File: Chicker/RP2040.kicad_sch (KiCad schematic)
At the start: 44 parts, among them J2 USB4145-03-0170-C_REVA2, J4 JST_2P_LIMITSW, J5 Conn_02x09_Counter_Clockwise, U1 RPI2040, U10 PTS647SM38SMTR2LFS, U5 W25Q16JVSNIQ, U9 PTS647SM38SMTR2LFS, Y1 ABM3-12.000MHZ-D2Y-T

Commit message: chicker v1.1 basic parts
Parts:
- removed D21, D22, D23, D24, D25: BZT52C3V3T-7, bots:D_SOD-523, symbol thebots_symlib:D_ZENER_BZT52C3V3T-7
- removed D5: SMBJ5338B-TP, bots:D_SMB, symbol bots:D_ZENER_SMBJ5338B-TP
- removed U10, U9: PTS647SM38SMTR2LFS, bots:SW_PTS647SM38SMTR2LFS_CNK, symbol bots:PTS647SM38SMTR2LFS
- removed U5: W25Q16JVSNIQ, bots:SOIC-8_3.9x4.9mm_P1.27mm, symbol bots:W25Q16JVSNIQ
- removed Y1: ABM3-12.000MHZ-D2Y-T, bots:ABM3, symbol bots:ABM3-12.000MHZ-D2Y-T
- added D21, D23: ESD7C3.3DT5G-MS, bots:SOT-723, symbol bots:D_TVS_ESD
- added D5: SMBJ5338B-TP_alternate, bots:D_SMB, symbol bots:D_ZENER_SMBJ5338B_alternate
- added U10, U9: SW_TS-1187A-B-A-B, bots:SW_TS-1187A-B-A-B, symbol bots:SW_TS-1187A-B-A-B
- added U5: W25Q128JVSIQ, bots:SOIC-8_208mil, symbol bots:W25Q128JVSIQ
- added Y1: XTAL-12MHZ-YXC, bots:SMD3225-4P, symbol bots:XTAL-12MHZ-YXC
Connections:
- net +3.3V: now also U5.8 (VCC)
- net 5V_LEVEL: now also D21.2
- net 5V_USB: now also D5.1 (K)
- net BATT_LEVEL: now also D21.1
- net BKBM: now also D23.1
- net BOOT: now also U10.1, U10.2
- net CHIP: now also D21.1
- net GND: now also D21.3, D23.3, D5.2 (A), U10.3, U10.4, U5.4 (GND), U9.3, U9.4, Y1.2, Y1.4
- net GPIO27_ADC2: now also D23.2
- net KICK: now also D21.2
- net QSPI_SCLK: now also U5.6 (CLK)
- net QSPI_SD0: now also U5.5 (DI(IO0))
- net QSPI_SD1: now also U5.2 (DO(IO1))
- net QSPI_SD2: now also U5.3 (IO2)
- net QSPI_SD3: now also U5.7 (IO3)
- net QSPI_SS: now also U5.1 (~{CS})
- net RUN: now also U9.1, U9.2
- net XIN: now also Y1.3
- net XOUT_R: now reaches C25.2, R17.1
- net XOUT_R: now also Y1.1
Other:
- moved on the sheet: R17

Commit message: more parts
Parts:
- added D21: ESD7C3.3DT5G-MS, bots:SOT-723, symbol bots:D_TVS_ESD
- renumbered D21 to D22
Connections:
- net CHIP: now also D21.1; no longer D22.1
- net GND: now also D21.3
- net KICK: now also D21.2; no longer D22.2

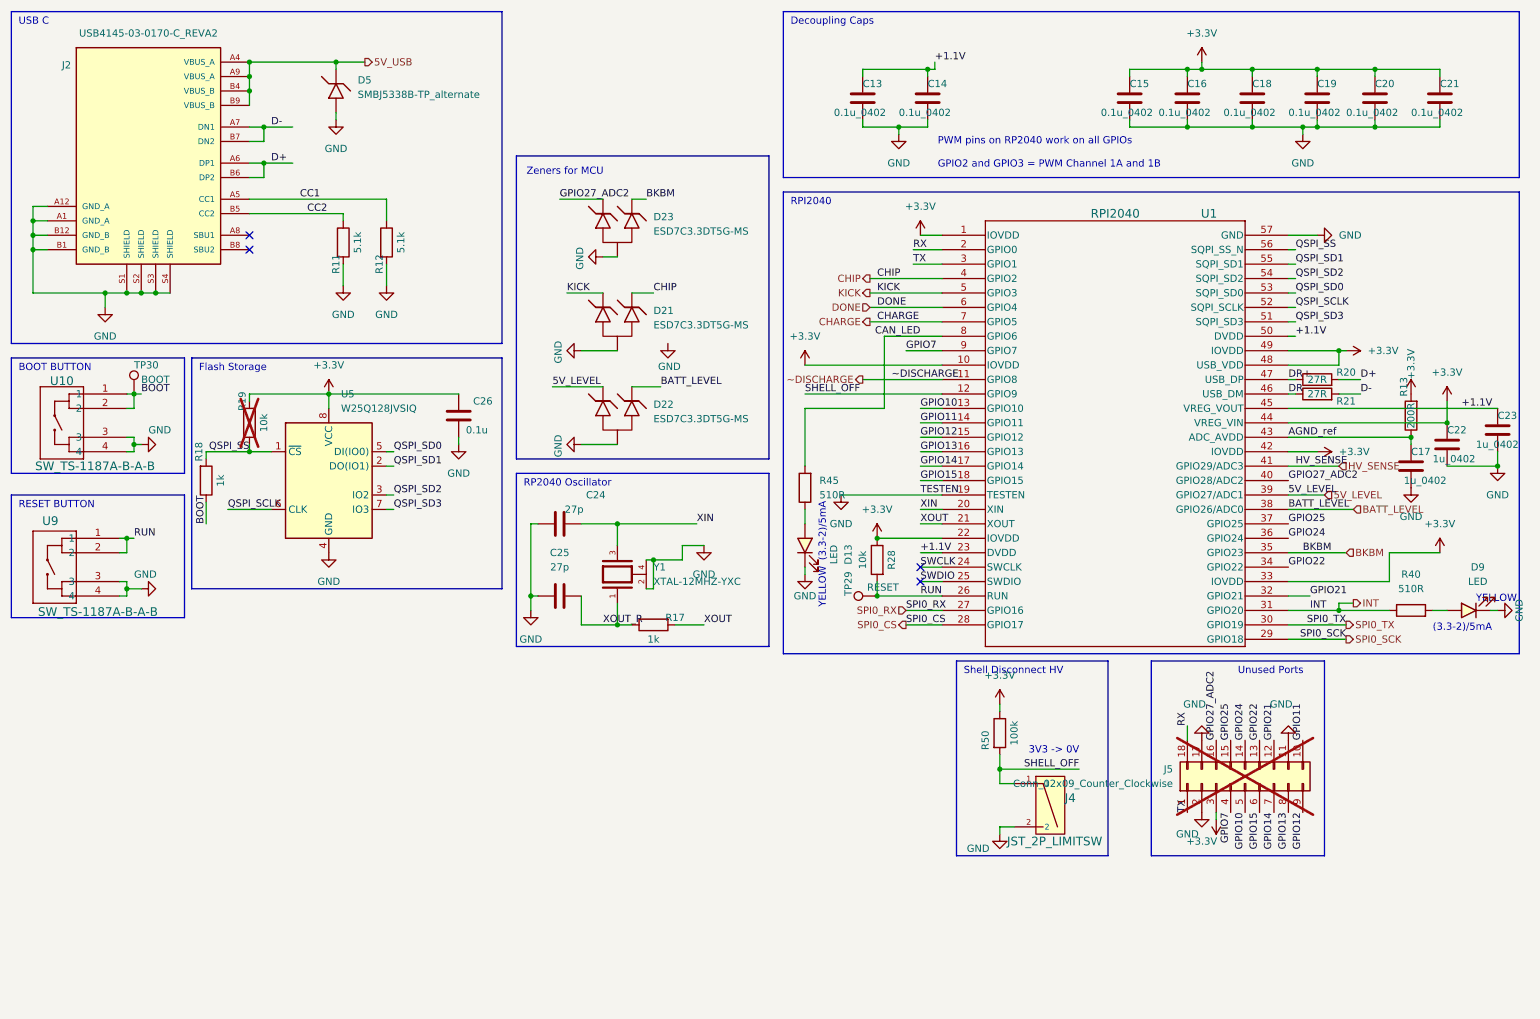
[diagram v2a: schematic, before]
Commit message: changed more to basic
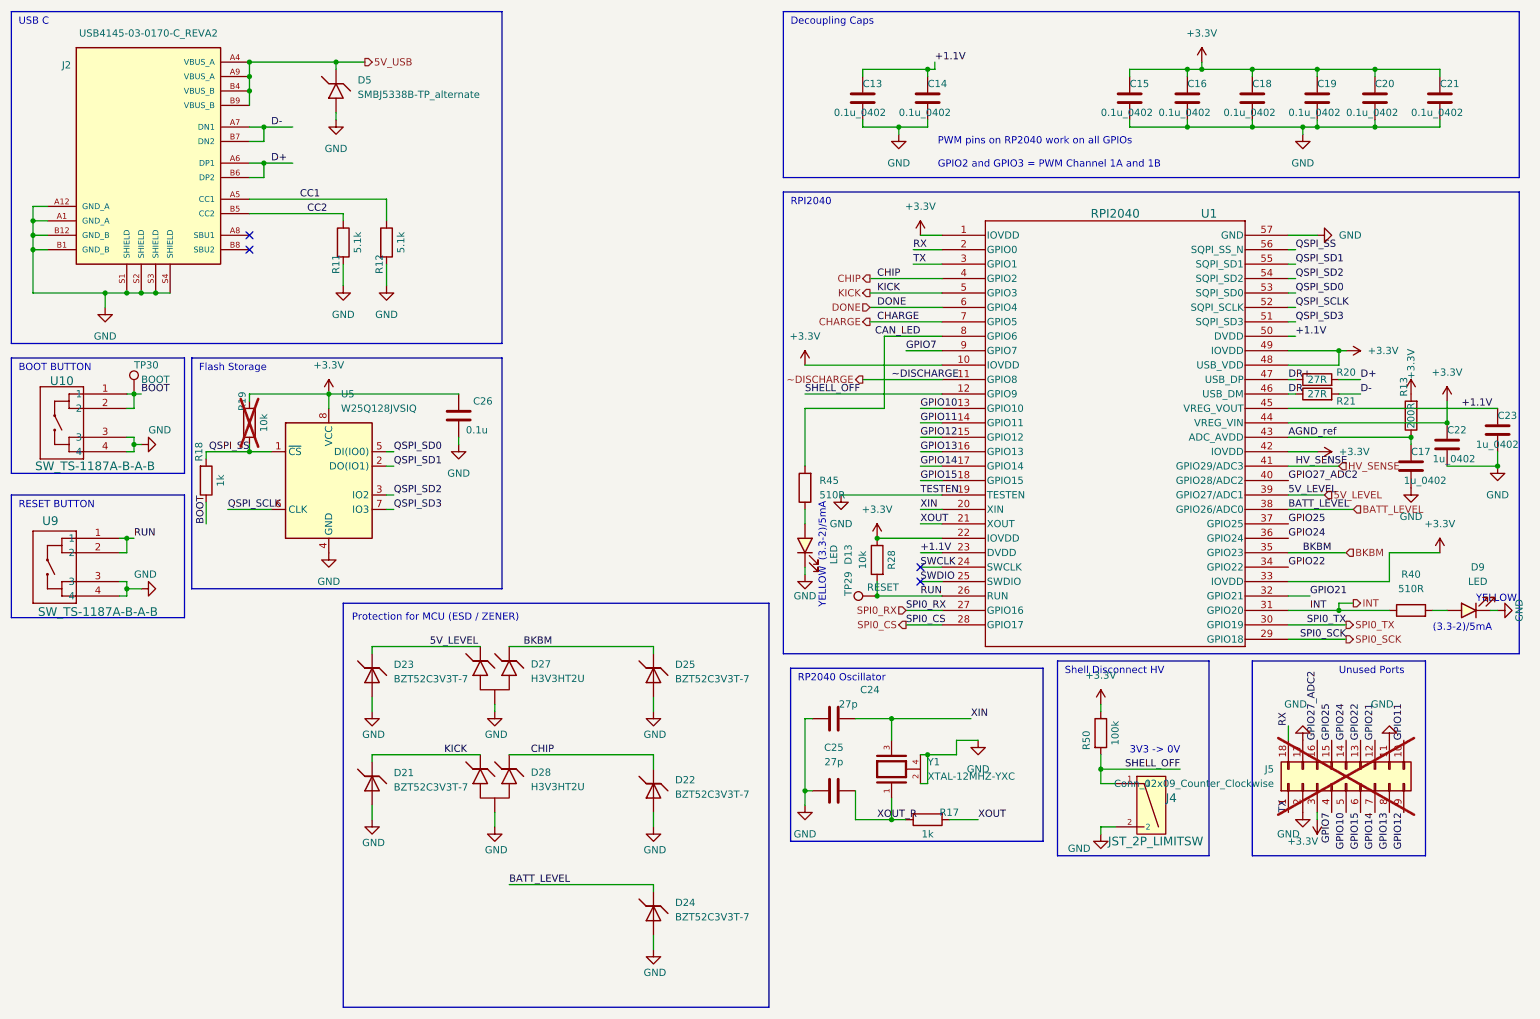
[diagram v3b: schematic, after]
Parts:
- removed D22: ESD7C3.3DT5G-MS, bots:SOT-723, symbol bots:D_TVS_ESD
- added D21, D22, D23, D24, D25: BZT52C3V3T-7, bots:D_SOD-523, symbol bots:D_ZENER_BZT52C3V3T-7_alternate
- D13, D9: footprint bots:LED_0603_1608Metric -> bots:LED_0805_2012Metric; JLC 0603 -> 0805; LCSC C72038 -> C2296; MPN 19-213/Y2C-CQ2R2L/3T(CY) -> KT-0805Y; Manufacturer Everlight Elec -> Hubei KENTO Elec
- D27: renamed from D23; value ESD7C3.3DT5G-MS -> H3V3HT2U; JLC SOT-723 -> SOT-23; LCSC C5331072 -> C20617924; MPN ESD7C3.3DT5G-MS -> H3V3HT2U; Manufacturer Micro Commercial Co -> hongjiacheng; Price 0.63 -> 0.0379
- D28: renamed from D21; value ESD7C3.3DT5G-MS -> H3V3HT2U; JLC SOT-723 -> SOT-23; LCSC C5331072 -> C20617924; MPN ESD7C3.3DT5G-MS -> H3V3HT2U; Manufacturer Micro Commercial Co -> hongjiacheng; Price 0.63 -> 0.0379
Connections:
- net 5V_LEVEL: now also D27.2, D23.1 (K)
- net BATT_LEVEL: now also D24.1 (K)
- net BKBM: now also D25.1 (K)
- net CHIP: now also D22.1 (K)
- net GND: now also D21.2 (A), D22.2 (A), D23.2 (A), D24.2 (A), D25.2 (A)
- net GPIO27_ADC2: no longer D27.2
- net KICK: now also D21.1 (K)
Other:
- note added: "Protection for MCU (ESD / ZENER)"
- note removed: "Zeners for MCU"
- moved on the sheet: C24, C25, D27, D28, J4, J5, R17, R50, Y1

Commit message: chicker v1.1 ordered!
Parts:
- removed J2: USB4145-03-0170-C_REVA2, bots:GCT_USB4145-03-0170-C_REVA2, symbol bots:USB4145-03-0170-C_REVA2
- removed R20, R21: 27R, bots:R_0603_1608Metric, symbol thebots_symlib:R_27R
- added J2: USB4145-03-0170-C, bots:GCT_USB4145-03-0170-C_REVA2, symbol bots:USB4145-03-0170-C
- added R20: 33R, bots:R_0603_1608Metric, symbol bots:R_33R
- D27, D28: footprint bots:SOT-723 -> bots:SOT-23
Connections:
- net 5V_USB: now also J2.A4 (VBUS_A), J2.A9 (VBUS_A), J2.B4 (VBUS_B), J2.B9 (VBUS_B)
- net CC1: now also J2.A5 (CC1)
- net CC2: now also J2.B5 (CC2)
- net D+: now also J2.A6 (DP1), J2.B6 (DP2), R20.2
- net D-: now also J2.A7 (DN1), J2.B7 (DN2), R20.2
- net DR+: now also R20.1
- net DR-: now also R20.1
- net GND: now also J2.A1 (GND_A), J2.A12 (GND_A), J2.B1 (GND_B), J2.B12 (GND_B), J2.S1 (SHIELD), J2.S2 (SHIELD), J2.S3 (SHIELD), J2.S4 (SHIELD)

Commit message: firmware + RCD snubber
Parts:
- added R20: 33R, bots:R_0603_1608Metric, symbol bots:R_33R
- renumbered R20 to R21
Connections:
- net D+: now also R20.2; no longer R21.2
- net DR+: now also R20.1; no longer R21.1

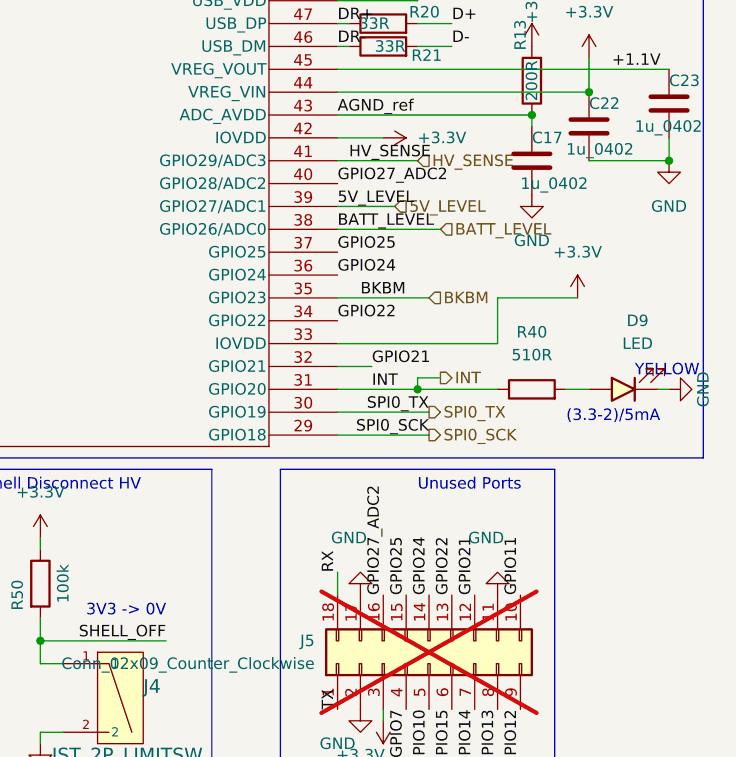
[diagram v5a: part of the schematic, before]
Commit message: pcb pin number change
(from last summer)
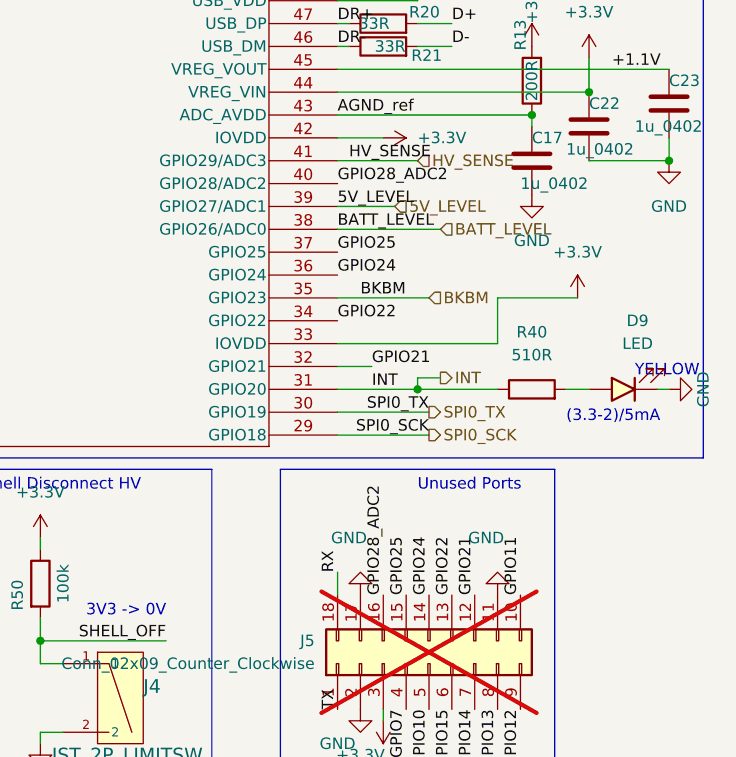
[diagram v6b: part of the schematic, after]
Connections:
- net GPIO27_ADC2 renamed GPIO28_ADC2
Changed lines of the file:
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@@
 		)
 	)
-	(label "GPIO27_ADC2"
+	(label "GPIO28_ADC2"
 		(at 238.76 97.79 0)
 		(effects
@@
 		)
 	)
-	(label "GPIO27_ADC2"
+	(label "GPIO28_ADC2"
 		(at 243.84 143.51 90)
 		(effects
